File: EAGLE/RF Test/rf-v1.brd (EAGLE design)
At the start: 20.3 x 35.6 mm, 9 parts, among them X1 SMA-142-0701-851/861, X2 IPEX-20279-001E

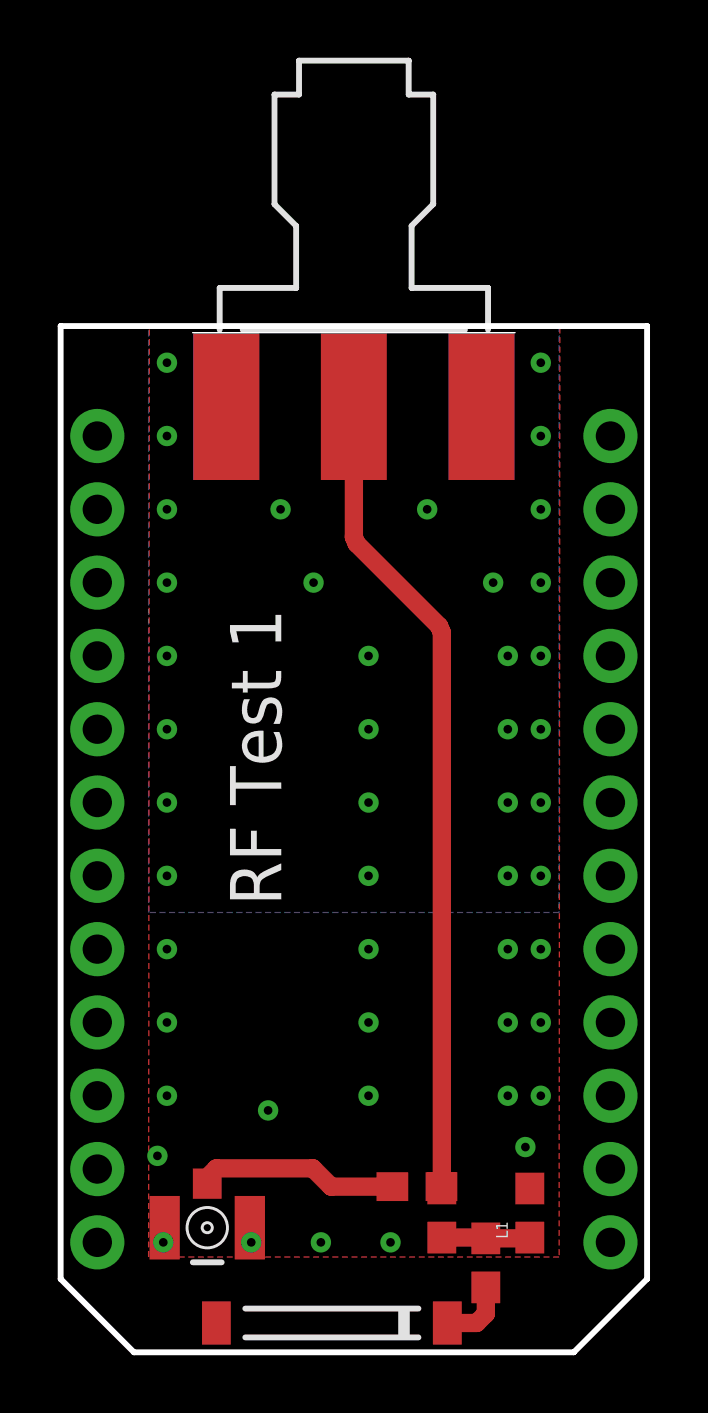
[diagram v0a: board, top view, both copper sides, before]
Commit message: Added RF test boards and their gerbers
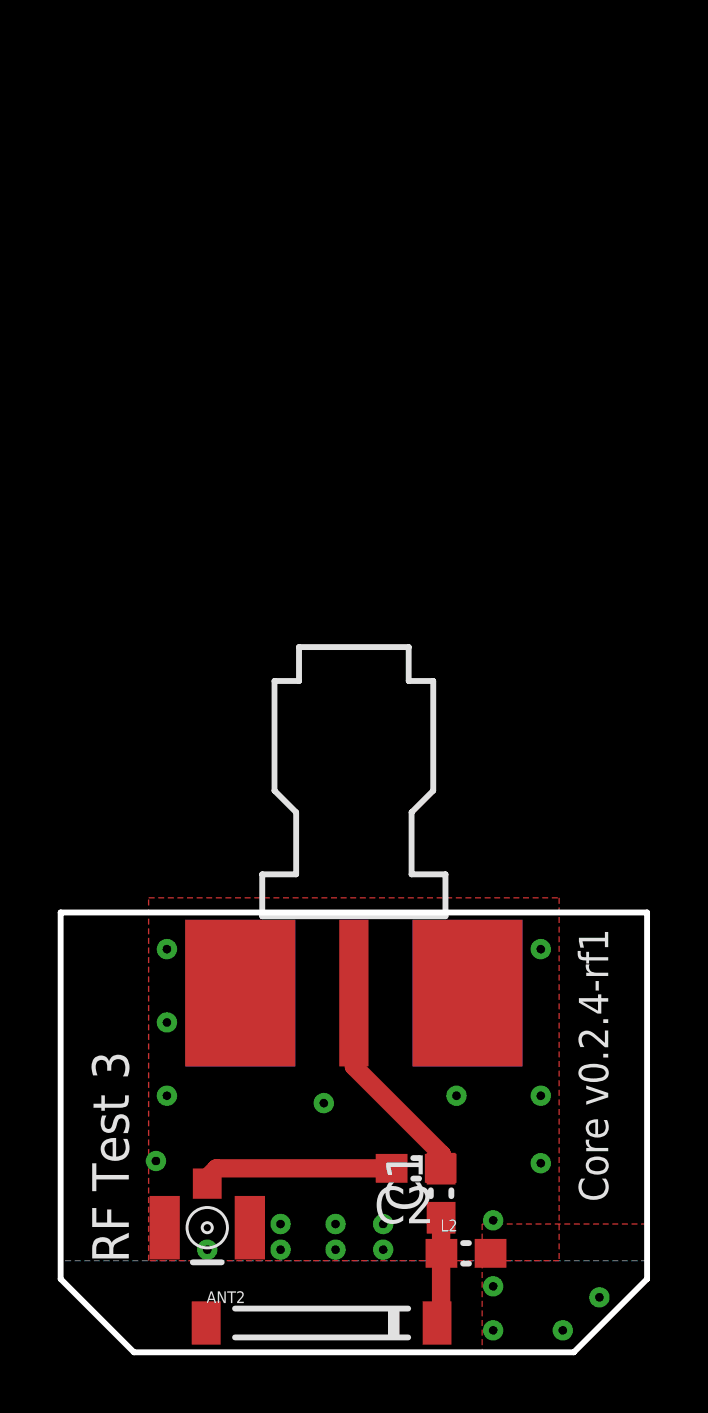
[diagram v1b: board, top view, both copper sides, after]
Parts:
- removed ANT1: AT8010, Spark:AT8010
- removed C12, C16: 10pF, rcl:C0603
- removed C4: 2.2pF, rcl:C0603
- removed JP1, JP2: (no value), SparkFun:1X12
- removed L1: 2.2nH, SparkFun-Passives:0603
- added ANT2: AT8010, Spark:AT8010
- added C1: 2.2pF, rcl:C0603
- added C2: 10pF, rcl:C0603
- added L2: 2.2nH, SparkFun-Passives:0603
- X1: value SMA-142-0701-851/861 -> SMA-142-0701-881/886; device con-coax:J502-ND-142-0701-851/861 -> andyw-oct-2011:ANDYW-GENERIC-END-LAUNCH
- moved X1 20.3 mm to (10.2, 12.5)
- renumbered X2 to X3
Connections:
- removed net !RST: JP2.2
- removed net +3V3: JP2.1
- removed net A0: JP1.12
- removed net A1: JP1.11
- removed net A2: JP1.10
- removed net A3: JP1.9
- removed net A4: JP1.8
- removed net A5: JP1.7
- removed net A6: JP1.6
- removed net A7: JP1.5
- removed net D0: JP2.12
- removed net D1: JP2.11
- removed net D2: JP2.10
- removed net D3: JP2.9
- removed net D4: JP2.8
- removed net D5: JP2.7
- removed net D6: JP2.6
- removed net D7: JP2.5
- removed net N$3: ANT1.SIG, C4.1
- removed net N$5: C12.1, C4.2, L1.1
- removed net RAW: JP1.1
- removed net RX: JP1.4
- removed net TX: JP1.3
- removed net VDDA: JP2.3
- new net N$1: ANT2.SIG, C1.1, L2.1
- new net N$6: C1.2, C2.1
- net GND: now also L2.2; no longer JP1.2, JP2.4, L1.2
- net N$2: now also C2.2; no longer C16.2
- net N$4: no longer C12.2, C16.1
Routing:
- net N$4: track 28.4 -> 2.29 mm
- net S$1: track 0.00 -> 4.82 mm
- net N$1: track 0.00 -> 3.72 mm
- net N$5: track 3.07 -> 0.00 mm
- net N$3: track 2.38 -> 0.00 mm
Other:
- board size 20.3 x 35.6 mm -> 20.3 x 15.2 mm
- board text added: "Core v0.2.4-rf1"
- board text added: "RF Test 3"
- board text removed: "RF Test 1"
